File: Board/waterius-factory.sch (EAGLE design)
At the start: 23 parts, among them IC1 TINY13-20SU, U2 MCP1700T-3302E/TT, U3 ESP01

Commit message: readme
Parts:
- added PAD1: MOUNT-HOLE2.8, holes:MOUNT-HOLE2.8
- JP1: value (none) -> + -
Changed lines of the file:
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@@
 <parts>
 <part name="U2" library="MCP1700T-3302E_TT" deviceset="MCP1700T-3302E/TT" device=""/>
-<part name="JP1" library="jumper" deviceset="JP1E" device=""/>
+<part name="JP1" library="jumper" deviceset="JP1E" device="" value="+ -"/>
 <part name="C1" library="rcl" deviceset="C-EU" device="C0805" value="1uF"/>
 <part name="C2" library="rcl" deviceset="C-EU" device="C0805" value="1uF"/>
@@
 <part name="C4" library="rcl" deviceset="C-EU" device="C0805" value="0.1uF"/>
 <part name="GND7" library="supply1" deviceset="GND" device=""/>
+<part name="PAD1" library="holes" library_urn="urn:adsk.eagle:library:237" deviceset="MOUNT-HOLE" device="2.8" package3d_urn="urn:adsk.eagle:package:14271/1"/>
 </parts>
 <sheets>
@@
 <instance part="C4" gate="G$1" x="76.2" y="15.24"/>
 <instance part="GND7" gate="1" x="76.2" y="2.54"/>
+<instance part="PAD1" gate="G$1" x="-35.56" y="106.68"/>
 </instances>
 <busses>
@@
 </schematic>
 </drawing>
+<compatibility>
+<note version="8.2" severity="warning">
+Since Version 8.2, EAGLE supports online libraries. The ids
+of those online libraries will not be understood (or retained)
+with this version.
+</note>
+<note version="8.3" severity="warning">
+Since Version 8.3, EAGLE supports URNs for individual library
+assets (packages, symbols, and devices). The URNs of those assets
+will not be understood (or retained) with this version.
+</note>
+<note version="8.3" severity="warning">
+Since Version 8.3, EAGLE supports the association of 3D packages
+with devices in libraries, schematics, and board files. Those 3D
+packages will not be understood (or retained) with this version.
+</note>
+</compatibility>
 </eagle>

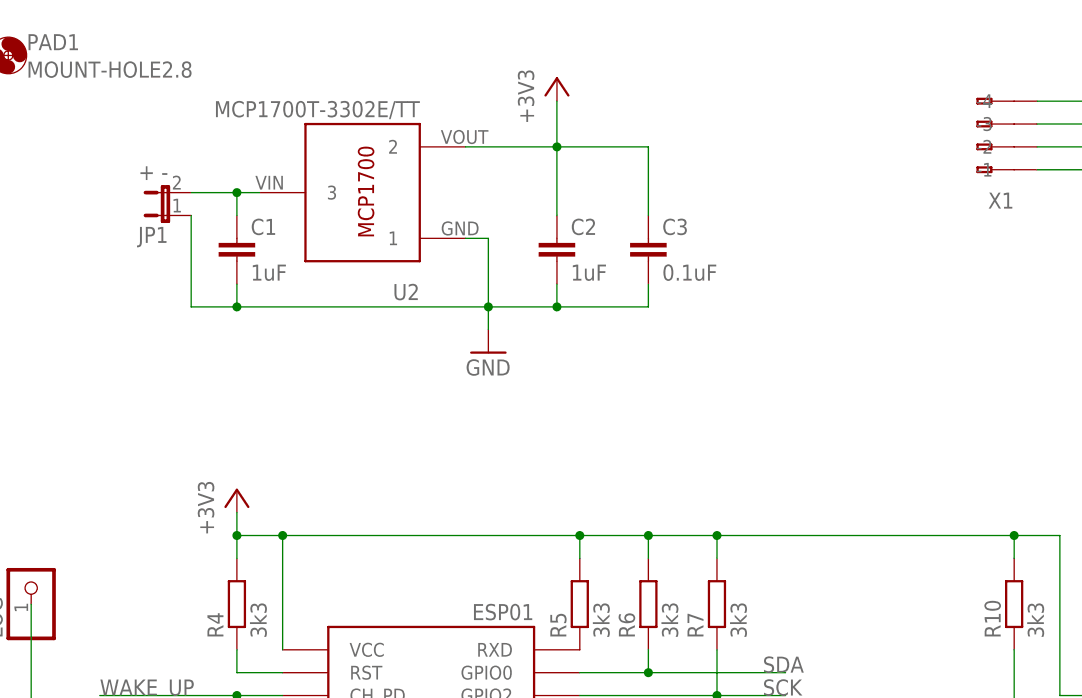
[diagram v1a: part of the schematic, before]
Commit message: 1. Добавлен U3 наверх и низ платы
2. подписан каждый пин ESP
3. Позиционные обозначения многие переставлены
4. В схеме изменён компонент на MCP1700-3002
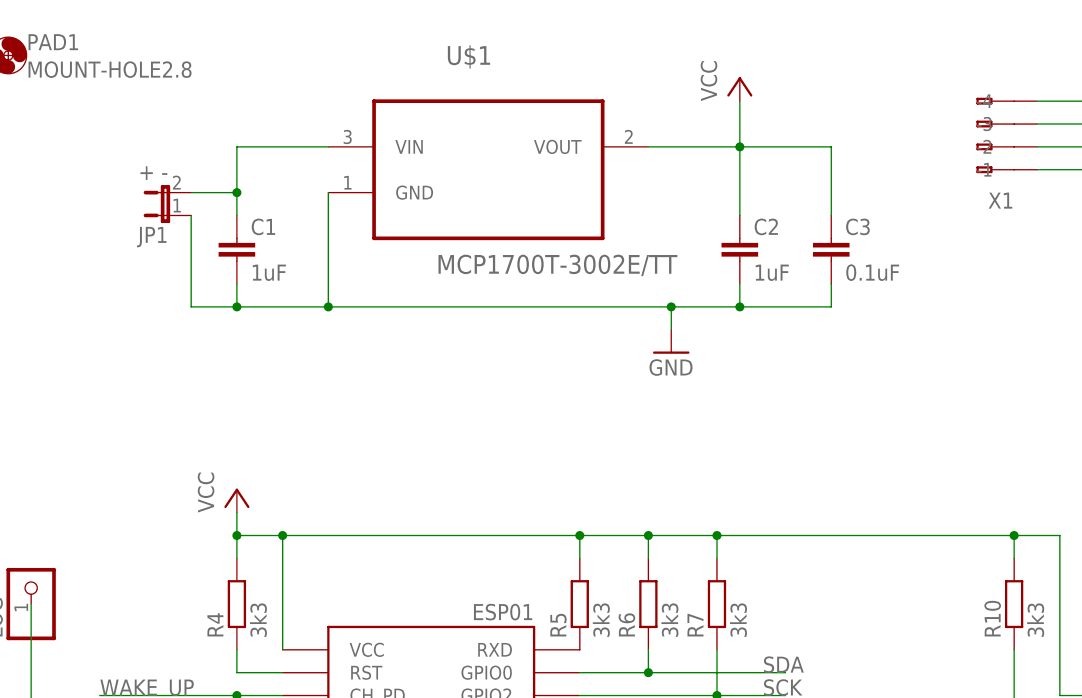
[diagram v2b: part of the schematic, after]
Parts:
- removed U2: MCP1700T-3302E/TT, MCP1700T-3302E_TT:MCP1700T-3302E/TT
- added U$1: MCP1700T-3002E/TT, Microchip_By_element14_Batch_1:MCP1700T-3002E/TT
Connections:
- removed net +3V3: C2.1, C3.1, IC1.VCC, R10.2, R4.2, R5.2, R6.2, R7.2, U2.2, U3.VCC
- new net +3V: C2.1, C3.1, IC1.VCC, R10.2, R4.2, R5.2, R6.2, R7.2, U$1.VOUT, U3.VCC
- net GND: now also U$1.GND; no longer U2.1
- net N$1: now also U$1.VIN; no longer U2.3
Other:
- moved on the sheet: C2, C3
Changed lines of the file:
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@@
 <?xml version="1.0" encoding="utf-8"?>
 <!DOCTYPE eagle SYSTEM "eagle.dtd">
-<eagle version="9.0.1">
+<eagle version="8.6.0">
 <drawing>
 <settings>
@@
 </classes>
 <parts>
-<part name="U2" library="MCP1700T-3302E_TT" deviceset="MCP1700T-3302E/TT" device=""/>
 <part name="JP1" library="jumper" deviceset="JP1E" device="" value="+ -"/>
 <part name="C1" library="rcl" deviceset="C-EU" device="C0805" value="1uF"/>
 <part name="C2" library="rcl" deviceset="C-EU" device="C0805" value="1uF"/>
 <part name="C3" library="rcl" deviceset="C-EU" device="C0805" value="0.1uF"/>
-<part name="+3V1" library="supply1" deviceset="+3V3" device=""/>
+<part name="+3V" library="supply1" library_urn="urn:adsk.eagle:library:371" deviceset="VCC" device=""/>
 <part name="X1" library="con-wago255" deviceset="233-104" device=""/>
 <part name="R1" library="resistor" deviceset="R-EU_" device="R0805" value="3k3"/>
 <part name="GND1" library="supply1" deviceset="GND" device=""/>
 <part name="GND2" library="supply1" deviceset="GND" device=""/>
-<part name="+3V2" library="supply1" deviceset="+3V3" device=""/>
+<part name="+3V2" library="supply1" library_urn="urn:adsk.eagle:library:371" deviceset="VCC" device=""/>
 <part name="LOG" library="pinhead" deviceset="PINHD-1X1" device=""/>
 <part name="R2" library="resistor" deviceset="R-EU_" device="R0805" value="300"/>
@@
 <part name="GND7" library="supply1" deviceset="GND" device=""/>
 <part name="PAD1" library="holes" library_urn="urn:adsk.eagle:library:237" deviceset="MOUNT-HOLE" device="2.8" package3d_urn="urn:adsk.eagle:package:14271/1"/>
+<part name="U$1" library="Microchip_By_element14_Batch_1" deviceset="MCP1700T-3002E/TT" device=""/>
 </parts>
 <sheets>
@@
 </plain>
 <instances>
-<instance part="U2" gate="G$1" x="10.16" y="99.06" rot="R180"/>
 <instance part="JP1" gate="A" x="-17.78" y="88.9" rot="R90"/>
 <instance part="C1" gate="G$1" x="-10.16" y="86.36"/>
-<instance part="C2" gate="G$1" x="25.4" y="86.36"/>
-<instance part="C3" gate="G$1" x="35.56" y="86.36"/>
-<instance part="+3V1" gate="G$1" x="25.4" y="104.14"/>
+<instance part="C2" gate="G$1" x="45.72" y="86.36"/>
+<instance part="C3" gate="G$1" x="55.88" y="86.36"/>
+<instance part="+3V" gate="VCC" x="45.72" y="104.14"/>
 <instance part="X1" gate="G$1" x="71.12" y="96.52" rot="R180"/>
 <instance part="R1" gate="G$1" x="96.52" y="106.68"/>
 <instance part="GND1" gate="1" x="106.68" y="91.44"/>
-<instance part="GND2" gate="1" x="17.78" y="73.66"/>
-<instance part="+3V2" gate="G$1" x="-10.16" y="58.42"/>
+<instance part="GND2" gate="1" x="38.1" y="73.66"/>
+<instance part="+3V2" gate="VCC" x="-10.16" y="58.42"/>
 <instance part="LOG" gate="G$1" x="-33.02" y="48.26" rot="R90"/>
 <instance part="R2" gate="G$1" x="96.52" y="96.52"/>
@@
 <instance part="GND7" gate="1" x="76.2" y="2.54"/>
 <instance part="PAD1" gate="G$1" x="-35.56" y="106.68"/>
+<instance part="U$1" gate="A" x="17.78" y="96.52"/>
 </instances>
 <busses>
@@
 <pinref part="C1" gate="G$1" pin="1"/>
 <wire x1="-10.16" y1="88.9" x2="-10.16" y2="91.44" width="0.1524" layer="91"/>
-<pinref part="U2" gate="G$1" pin="3"/>
-<wire x1="-10.16" y1="91.44" x2="-7.62" y2="91.44" width="0.1524" layer="91"/>
+<wire x1="-10.16" y1="91.44" x2="-10.16" y2="96.52" width="0.1524" layer="91"/>
 <junction x="-10.16" y="91.44"/>
-</segment>
-</net>
-<net name="+3V3" class="0">
-<segment>
-<pinref part="U2" gate="G$1" pin="2"/>
-<wire x1="15.24" y1="96.52" x2="25.4" y2="96.52" width="0.1524" layer="91"/>
-<pinref part="+3V1" gate="G$1" pin="+3V3"/>
-<wire x1="25.4" y1="96.52" x2="25.4" y2="101.6" width="0.1524" layer="91"/>
+<pinref part="U$1" gate="A" pin="VIN"/>
+<wire x1="-10.16" y1="96.52" x2="0" y2="96.52" width="0.1524" layer="91"/>
+</segment>
+</net>
+<net name="+3V" class="0">
+<segment>
+<wire x1="35.56" y1="96.52" x2="45.72" y2="96.52" width="0.1524" layer="91"/>
+<pinref part="+3V" gate="VCC" pin="VCC"/>
+<wire x1="45.72" y1="96.52" x2="45.72" y2="101.6" width="0.1524" layer="91"/>
 <pinref part="C2" gate="G$1" pin="1"/>
-<wire x1="25.4" y1="88.9" x2="25.4" y2="96.52" width="0.1524" layer="91"/>
-<junction x="25.4" y="96.52"/>
+<wire x1="45.72" y1="88.9" x2="45.72" y2="96.52" width="0.1524" layer="91"/>
+<junction x="45.72" y="96.52"/>
 <pinref part="C3" gate="G$1" pin="1"/>
-<wire x1="35.56" y1="88.9" x2="35.56" y2="96.52" width="0.1524" layer="91"/>
-<wire x1="35.56" y1="96.52" x2="25.4" y2="96.52" width="0.1524" layer="91"/>
+<wire x1="55.88" y1="88.9" x2="55.88" y2="96.52" width="0.1524" layer="91"/>
+<wire x1="55.88" y1="96.52" x2="45.72" y2="96.52" width="0.1524" layer="91"/>
+<pinref part="U$1" gate="A" pin="VOUT"/>
 </segment>
 <segment>
 <pinref part="R4" gate="G$1" pin="2"/>
-<pinref part="+3V2" gate="G$1" pin="+3V3"/>
+<pinref part="+3V2" gate="VCC" pin="VCC"/>
 <wire x1="-10.16" y1="50.8" x2="-10.16" y2="53.34" width="0.1524" layer="91"/>
 <wire x1="-10.16" y1="53.34" x2="-10.16" y2="55.88" width="0.1524" layer="91"/>
@@
 <wire x1="-10.16" y1="78.74" x2="-10.16" y2="81.28" width="0.1524" layer="91"/>
 <pinref part="C2" gate="G$1" pin="2"/>
-<wire x1="25.4" y1="81.28" x2="25.4" y2="78.74" width="0.1524" layer="91"/>
-<wire x1="25.4" y1="78.74" x2="17.78" y2="78.74" width="0.1524" layer="91"/>
+<wire x1="45.72" y1="81.28" x2="45.72" y2="78.74" width="0.1524" layer="91"/>
+<wire x1="45.72" y1="78.74" x2="38.1" y2="78.74" width="0.1524" layer="91"/>
 <junction x="-10.16" y="78.74"/>
 <pinref part="C3" gate="G$1" pin="2"/>
-<wire x1="17.78" y1="78.74" x2="-10.16" y2="78.74" width="0.1524" layer="91"/>
-<wire x1="35.56" y1="81.28" x2="35.56" y2="78.74" width="0.1524" layer="91"/>
-<wire x1="35.56" y1="78.74" x2="25.4" y2="78.74" width="0.1524" layer="91"/>
-<junction x="25.4" y="78.74"/>
-<pinref part="U2" gate="G$1" pin="1"/>
-<wire x1="15.24" y1="86.36" x2="17.78" y2="86.36" width="0.1524" layer="91"/>
-<wire x1="17.78" y1="86.36" x2="17.78" y2="78.74" width="0.1524" layer="91"/>
-<junction x="17.78" y="78.74"/>
+<wire x1="38.1" y1="78.74" x2="0" y2="78.74" width="0.1524" layer="91"/>
+<wire x1="0" y1="78.74" x2="-10.16" y2="78.74" width="0.1524" layer="91"/>
+<wire x1="55.88" y1="81.28" x2="55.88" y2="78.74" width="0.1524" layer="91"/>
+<wire x1="55.88" y1="78.74" x2="45.72" y2="78.74" width="0.1524" layer="91"/>
+<junction x="45.72" y="78.74"/>
+<junction x="38.1" y="78.74"/>
 <pinref part="GND2" gate="1" pin="GND"/>
-<wire x1="17.78" y1="76.2" x2="17.78" y2="78.74" width="0.1524" layer="91"/>
-</segment>
-<segment>
+<wire x1="38.1" y1="76.2" x2="38.1" y2="78.74" width="0.1524" layer="91"/>
+<pinref part="U$1" gate="A" pin="GND"/>
+<wire x1="0" y1="91.44" x2="0" y2="78.74" width="0.1524" layer="91"/>
+<junction x="0" y="78.74"/>
+</segment>
+<segment>
